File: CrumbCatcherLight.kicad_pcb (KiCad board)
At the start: 2 copper layers, 60.1 x 69.1 mm, 72 parts, among them J1 USB_C_Receptacle, J2 Conn_ARM_SWD_TagConnect_TC203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, Q1 2N7002VC-7, SW1 TL3780AF240QG, SW10 SW_SPST, SW11 PEC11R, SW2 PEC11R, SW3 SW_SPST, SW4 SW_SPST, SW5 PEC11R, SW6 SW_SPST, SW7 SW_SPST, SW9 SW_SPST, U1 ECMF02-2AMX6, U2 PCB, U3 XC6210B332MR, U4 GD25Q127CWIGR, U5 RP2040, Y1 12MHz

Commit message: Update BOM,
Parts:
- removed C14: 22pF, Capacitor_SMD:C_0402_1005Metric
- removed C28, C29: 100nF, Capacitor_SMD:C_0402_1005Metric
- removed the SW1 at (47.6, 36.1)
- removed TP1: Reset, TestPoint:TestPoint_Pad_D1.0mm
- removed TP2: Delay, TestPoint:TestPoint_Pad_D1.0mm
- removed TP3: Boot, TestPoint:TestPoint_Pad_D1.0mm
- removed U2: PCB, Mad_Footprints:BOM
- removed Y1: 12MHz, Crystal:Crystal_SMD_Abracon_ABM8G-4Pin_3.2x2.5mm
- added C22: 1uF, Capacitor_SMD:C_0603_1608Metric, B.Cu at (140.4, 83.0)
- added C23: 100nF, Capacitor_SMD:C_0402_1005Metric, B.Cu at (145.2, 74.1)
- added C24: 100nF, Capacitor_SMD:C_0402_1005Metric, B.Cu at (147.2, 74.1)
- added C25: 100nF, Capacitor_SMD:C_0402_1005Metric, B.Cu at (149.2, 74.1)
- added D11: SK6812_MINI_E, Mad_Footprints:SK6812_MINI_E, F.Cu at (139.5, 25.2)
- added D12: LL4148, Diode_SMD:D_MiniMELF, F.Cu at (146.8, 24.0)
- added D13: LL4148, Diode_SMD:D_MiniMELF, F.Cu at (146.8, 27.3)
- added D14: LL4148, Diode_SMD:D_MiniMELF, F.Cu at (146.8, 30.7)
- added D15: SK6812_MINI_E, Mad_Footprints:SK6812_MINI_E, F.Cu at (139.5, 31.0)
- added D16: SK6812_MINI_E, Mad_Footprints:SK6812_MINI_E, F.Cu at (139.5, 36.8)
- added D17: LL4148, Diode_SMD:D_MiniMELF, F.Cu at (146.8, 34.0)
- added D18: RB520S30, Diode_SMD:D_SOD-523, B.Cu at (105.6, 28.8)
- added R14: 27R, Resistor_SMD:R_0402_1005Metric, B.Cu at (120.1, 83.7)
- added SW10: TL3780AF240QG, Mad_Footprints:SW_TL3780AF240QG, B.Cu at (102.3, 31.3)
- added U0: PCB, Mad_Footprints:BOM, F.Cu at (154.0, 35.5)
- added X1: ECS-2520MVLC-120-CN, Mad_Footprints:Crystal_SMD_ECX-32-4Pin_3.2x2.5mm, B.Cu at (155.4, 78.2)
- C15: value 22pF -> 10uF; footprint Capacitor_SMD:C_0402_1005Metric -> Capacitor_SMD:C_0805_2012Metric
- C16: value 100nF -> 10uF; footprint Capacitor_SMD:C_0402_1005Metric -> Capacitor_SMD:C_0805_2012Metric
- C20: value 100nF -> 1uF; footprint Capacitor_SMD:C_0402_1005Metric -> Capacitor_SMD:C_0603_1608Metric
- C3, C4: footprint Capacitor_SMD:C_0402_1005Metric -> Capacitor_SMD:C_0805_2012Metric
- C5: value 4.7uF -> 10uF
- C6: value 10uF -> 100nF
- C7: value 10uF -> 100nF; footprint Capacitor_SMD:C_0805_2012Metric -> Capacitor_SMD:C_0402_1005Metric
- D1: value RB520S30 -> SK6812_MINI_E; footprint Diode_SMD:D_SOD-523 -> Mad_Footprints:WS2812C-2020
- D10, D5, D6: value LL4148 -> SK6812_MINI_E; footprint Diode_SMD:D_MiniMELF -> Mad_Footprints:SK6812_MINI_E
- D2: value LL4148 -> LED; footprint Diode_SMD:D_MiniMELF -> LED_SMD:LED_0603_1608Metric; moved to B.Cu
- R10: value 27R -> 1K
- R11: value 1K -> 10K
- R12: value 2K2 -> 1K
- R13: value 5K1 -> 27R
- R3: value 10K -> 2K2
- R4: value 10K -> 5K1
- R5: value 51K -> 2K2
- R6: value 100K -> 10K
- R8: value 1K -> 51K
- R9: value 27R -> 100K
- U3: value XC6210B332MR -> NCP1117-3.3_SOT223; footprint Package_TO_SOT_SMD:SOT-23-5 -> Package_TO_SOT_SMD:SOT-223-3_TabPin2
- moved D1 112.7 mm to (156.8, 74.2)
- moved C17 80.3 mm to (152.7, 74.3)
- moved C18 78.7 mm to (152.9, 73.2)
- moved C19 78.7 mm to (152.9, 75.2)
- moved C13 78.0 mm to (153.2, 77.9), turned to -90 degrees
- moved C5 76.4 mm to (124.4, 74.8), turned to 90 degrees
- moved C4 66.2 mm to (122.6, 81.4), turned to -90 degrees
- moved R5 65.4 mm to (111.5, 62.2), turned to -90 degrees
- moved R11 64.8 mm to (108.2, 27.4)
- moved C15 64.8 mm to (109.7, 27.9)
- moved U3 64.5 mm to (119.0, 76.0)
- moved R3 64.0 mm to (86.6, 92.5)
- moved C6 62.0 mm to (82.4, 45.0)
- moved R4 56.8 mm to (88.5, 92.5)
- moved R9 55.9 mm to (113.1, 29.6)
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- renumbered SW2 to SW1, SW3 to SW2, SW4 to SW3, SW5 to SW4, SW6 to SW5, SW7 to SW6, SW11 to SW7, SW9 to SW8, SW10 to SW9
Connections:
- net /2_SDA1 renamed /RP2040a/SDA1
- net /3_SCL1 renamed /RP2040a/SCL1
- net /DATA_RX0 renamed /RP2040a/RX0
- net /RP2040/GPIO10 renamed /RP2040a/IO_10
- net /RP2040/GPIO17 renamed /RP2040a/RP2040/GPIO17
- net /RP2040/GPIO18 renamed /RP2040a/RP2040/GPIO18
- net /RP2040/GPIO20 renamed /RP2040a/MISO
- net /RP2040/GPIO21 renamed /RP2040a/~{CS}
- net /RP2040/GPIO22 renamed /RP2040a/SCK
- net /RP2040/GPIO23 renamed /RP2040a/MOSI
- net /RP2040/GPIO24 renamed /RP2040a/RP2040/GPIO24
- net /RP2040/GPIO26 renamed /RP2040a/A0
- net /RP2040/GPIO27 renamed /RP2040a/A1
- net /RP2040/GPIO28 renamed /RP2040a/A2
- net /RP2040/GPIO29 renamed /RP2040a/A3
- net /RP2040/GPIO7 renamed /RP2040a/IO_7
- net /RP2040/GPIO8 renamed /RP2040a/IO_8
- net /RP2040/GPIO9 renamed /RP2040a/IO_9
- net /RP2040/QSPI_SCLK renamed /RP2040a/RP2040/QSPI_SCLK
- net /RP2040/QSPI_SD0 renamed /RP2040a/RP2040/QSPI_SD0
- net /RP2040/QSPI_SD1 renamed /RP2040a/RP2040/QSPI_SD1
- net /RP2040/QSPI_SD2 renamed /RP2040a/RP2040/QSPI_SD2
- net /RP2040/QSPI_SD3 renamed /RP2040a/RP2040/QSPI_SD3
- net /RP2040/SWCLK renamed /RP2040a/SWCLK
- net /RP2040/SWDIO renamed /RP2040a/SWDIO
- C10 pad 1: /RP2040/3V3 -> /RP2040a/ENC3A
- C11 pad 1: /RP2040/3V3 -> GND
- C11 pad 2: GND -> /RP2040a/ENC3B
- C12 pad 1: /RP2040/3V3 -> /RP2040a/3V3
- C13 pad 1: /RP2040/3V3 -> /RP2040a/3V3
- C15 pad 1: GND -> Net-(Q1B-G)
- C15 pad 2: Net-(C15-Pad2) -> GND
- C16 pad 1: /RP2040/3V3 -> Net-(Q1B-G)
- C17 pad 1: /RP2040/3V3 -> /RP2040a/3V3
- C18 pad 1: /RP2040/1V1 -> /RP2040a/3V3
- C19 pad 1: /RP2040/1V1 -> /RP2040a/3V3
- C20 pad 1: /RP2040/GPIO15 -> GND
- C20 pad 2: GND -> /RP2040a/RP2040/1V1
- C21 pad 1: GND -> /RP2040a/3V3
- C21 pad 2: /RP2040/GPIO16 -> GND
- C26 pad 1: /RP2040/GPIO13 -> /RP2040a/RP2040/1V1
- C27 pad 1: GND -> /RP2040a/RP2040/1V1
- C27 pad 2: /RP2040/GPIO14 -> GND
- C5 pad 1: Net-(Q1B-G) -> /RP2040a/3V3
- C6 pad 1: /RP2040/3V3 -> /RP2040a/ENC1A
- C7 pad 1: Net-(Q1B-G) -> GND
- C7 pad 2: GND -> /RP2040a/ENC1B
- C8 pad 1: /RP2040/3V3 -> /RP2040a/ENC2A
- C9 pad 1: /RP2040/3V3 -> GND
- C9 pad 2: GND -> /RP2040a/ENC2B
- D1 pad 1: Net-(D1-K) -> unconnected-(D1-DOUT-Pad1)
- D1 pad 2: Net-(D1-A) -> GND
- D10 pad 1: /RP2040/GPIO6 -> +5V
- D10 pad 2: Net-(D10-A) -> Net-(D10-DOUT)
- D2 pad 1: /RP2040/GPIO4 -> GND
- D3 pad 1: /RP2040/GPIO5 -> /RP2040a/IO_5
- D4 pad 1: /RP2040/GPIO6 -> /RP2040a/IO_6
- D5 pad 1: /RP2040/GPIO4 -> +5V
- D5 pad 2: Net-(D5-A) -> Net-(D10-DIN)
- D6 pad 1: /RP2040/GPIO5 -> +5V
- D6 pad 2: Net-(D6-A) -> Net-(D11-DIN)
- D7 pad 1: /RP2040/GPIO6 -> /RP2040a/IO_4
- D8 pad 1: /RP2040/GPIO4 -> /RP2040a/IO_5
- D9 pad 1: /RP2040/GPIO5 -> /RP2040a/IO_6
- J2 pad 1: /RP2040/3V3 -> /RP2040a/3V3
- J2 pad 3: /RP2040/~{RST} -> /RP2040a/~{RST}
- Q1 pad 2: Net-(D1-A) -> Net-(D18-A)
- Q1 pad 6: /RP2040/~{RST} -> /RP2040a/~{RST}
- R10 pad 1: /RP2040/USB_D- -> /RP2040a/RP2040/XTAL_IN
- R10 pad 2: Net-(U5-D-) -> Net-(X1-OUT)
- R11 pad 1: Net-(C15-Pad2) -> /RP2040a/RP2040/QSPI_~{CS}
- R11 pad 2: Net-(U5-XTAL_OUT) -> /RP2040a/3V3
- R12 pad 1: VBUS -> Net-(Q1B-S)
- R12 pad 2: /RP2040/VBUS_DETECT -> /RP2040a/RP2040/QSPI_~{CS}
- R13 pad 1: /RP2040/VBUS_DETECT -> /RP2040a/USB_D+
- R13 pad 2: GND -> Net-(U5-D+)
- R3 pad 1: GND -> VBUS
- R3 pad 2: Net-(D1-A) -> /RP2040a/VBUS_DETECT
- R4 pad 1: /RP2040/~{RST} -> /RP2040a/VBUS_DETECT
- R4 pad 2: /RP2040/3V3 -> GND
- R5 pad 1: Net-(Q1B-G) -> /RP2040a/3V3
- R5 pad 2: Net-(D1-K) -> Net-(D2-A)
- R6 pad 2: Net-(Q1B-G) -> Net-(D18-A)
- R7 pad 1: /RP2040/QSPI_nCS -> /RP2040a/~{RST}
- R7 pad 2: /RP2040/3V3 -> /RP2040a/3V3
- R8 pad 1: Net-(Q1B-S) -> Net-(Q1B-G)
- R8 pad 2: /RP2040/QSPI_nCS -> Net-(D18-K)
- R9 pad 1: /RP2040/USB_D+ -> GND
- R9 pad 2: Net-(U5-D+) -> Net-(Q1B-G)
- SW1 pad A: /RP2040/GPIO11 -> /RP2040a/ENC1A
- SW1 pad B: /RP2040/GPIO12 -> /RP2040a/ENC1B
- SW1 pad S2: Net-(D2-A) -> Net-(D7-A)
- SW4 pad A: /RP2040/GPIO13 -> /RP2040a/ENC2A
- SW4 pad B: /RP2040/GPIO14 -> /RP2040a/ENC2B
- SW4 pad S2: Net-(D5-A) -> Net-(D12-A)
- SW5 pad 1: Net-(D7-A) -> Net-(D9-A)
- SW6 pad 1: Net-(D6-A) -> Net-(D8-A)
- SW7 pad A: /RP2040/GPIO15 -> /RP2040a/ENC3A
- SW7 pad B: /RP2040/GPIO16 -> /RP2040a/ENC3B
- SW7 pad S2: Net-(D8-A) -> Net-(D17-A)
- SW8 pad 1: Net-(D9-A) -> Net-(D13-A)
- SW9 pad 1: Net-(D10-A) -> Net-(D14-A)
- U1 pad 5: /RP2040/USB_D+ -> /RP2040a/USB_D-
- U1 pad 6: /RP2040/USB_D- -> /RP2040a/USB_D+
- U3 pad 1: +5V -> GND
- U3 pad 2: GND -> /RP2040a/3V3
- U4 pad 1: /RP2040/QSPI_nCS -> /RP2040a/RP2040/QSPI_~{CS}
- U4 pad 8: /RP2040/3V3 -> /RP2040a/3V3
- U5 pad 1: /RP2040/3V3 -> /RP2040a/3V3
- U5 pad 10: /RP2040/3V3 -> /RP2040a/3V3
- U5 pad 14: /RP2040/GPIO11 -> /RP2040a/ENC1A
- U5 pad 15: /RP2040/GPIO12 -> /RP2040a/ENC1B
- U5 pad 16: /RP2040/GPIO13 -> /RP2040a/ENC2A
- U5 pad 17: /RP2040/GPIO14 -> /RP2040a/ENC2B
- U5 pad 18: /RP2040/GPIO15 -> /RP2040a/ENC3A
- U5 pad 2: /LED_TX0 -> /RP2040a/TX0
- U5 pad 20: Net-(U5-XTAL_IN) -> /RP2040a/RP2040/XTAL_IN
- U5 pad 21: Net-(U5-XTAL_OUT) -> unconnected-(U5-XTAL_OUT-Pad21)
- U5 pad 22: /RP2040/3V3 -> /RP2040a/3V3
- U5 pad 23: /RP2040/1V1 -> /RP2040a/RP2040/1V1
- U5 pad 26: /RP2040/~{RST} -> /RP2040a/~{RST}
- U5 pad 27: /RP2040/GPIO16 -> /RP2040a/ENC3B
- U5 pad 30: /RP2040/VBUS_DETECT -> /RP2040a/VBUS_DETECT
- U5 pad 33: /RP2040/3V3 -> /RP2040a/3V3
- U5 pad 37: /RP2040/GPIO25 -> /RP2040a/STATUS_LED_DO
- U5 pad 42: /RP2040/3V3 -> /RP2040a/3V3
- U5 pad 43: /RP2040/3V3 -> /RP2040a/3V3
- U5 pad 44: /RP2040/3V3 -> /RP2040a/3V3
- U5 pad 45: /RP2040/1V1 -> /RP2040a/RP2040/1V1
- U5 pad 48: /RP2040/3V3 -> /RP2040a/3V3
- U5 pad 49: /RP2040/3V3 -> /RP2040a/3V3
- U5 pad 50: /RP2040/1V1 -> /RP2040a/RP2040/1V1
- U5 pad 56: /RP2040/QSPI_nCS -> /RP2040a/RP2040/QSPI_~{CS}
- U5 pad 6: /RP2040/GPIO4 -> /RP2040a/IO_4
- U5 pad 7: /RP2040/GPIO5 -> /RP2040a/IO_5
- U5 pad 8: /RP2040/GPIO6 -> /RP2040a/IO_6
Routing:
- net Net-(U5-XTAL_IN): track 8.23 -> 0.00 mm
- net /RP2040a/3V3: track 0.00 -> 3.18 mm
- net Net-(C15-Pad2): track 2.89 -> 0.00 mm
- net GND: track 6.16 -> 3.47 mm
- net Net-(U5-XTAL_OUT): track 1.93 -> 0.00 mm
- net /RP2040a/RP2040/XTAL_IN: track 0.00 -> 1.55 mm
- net Net-(X1-OUT): track 0.00 -> 1.27 mm

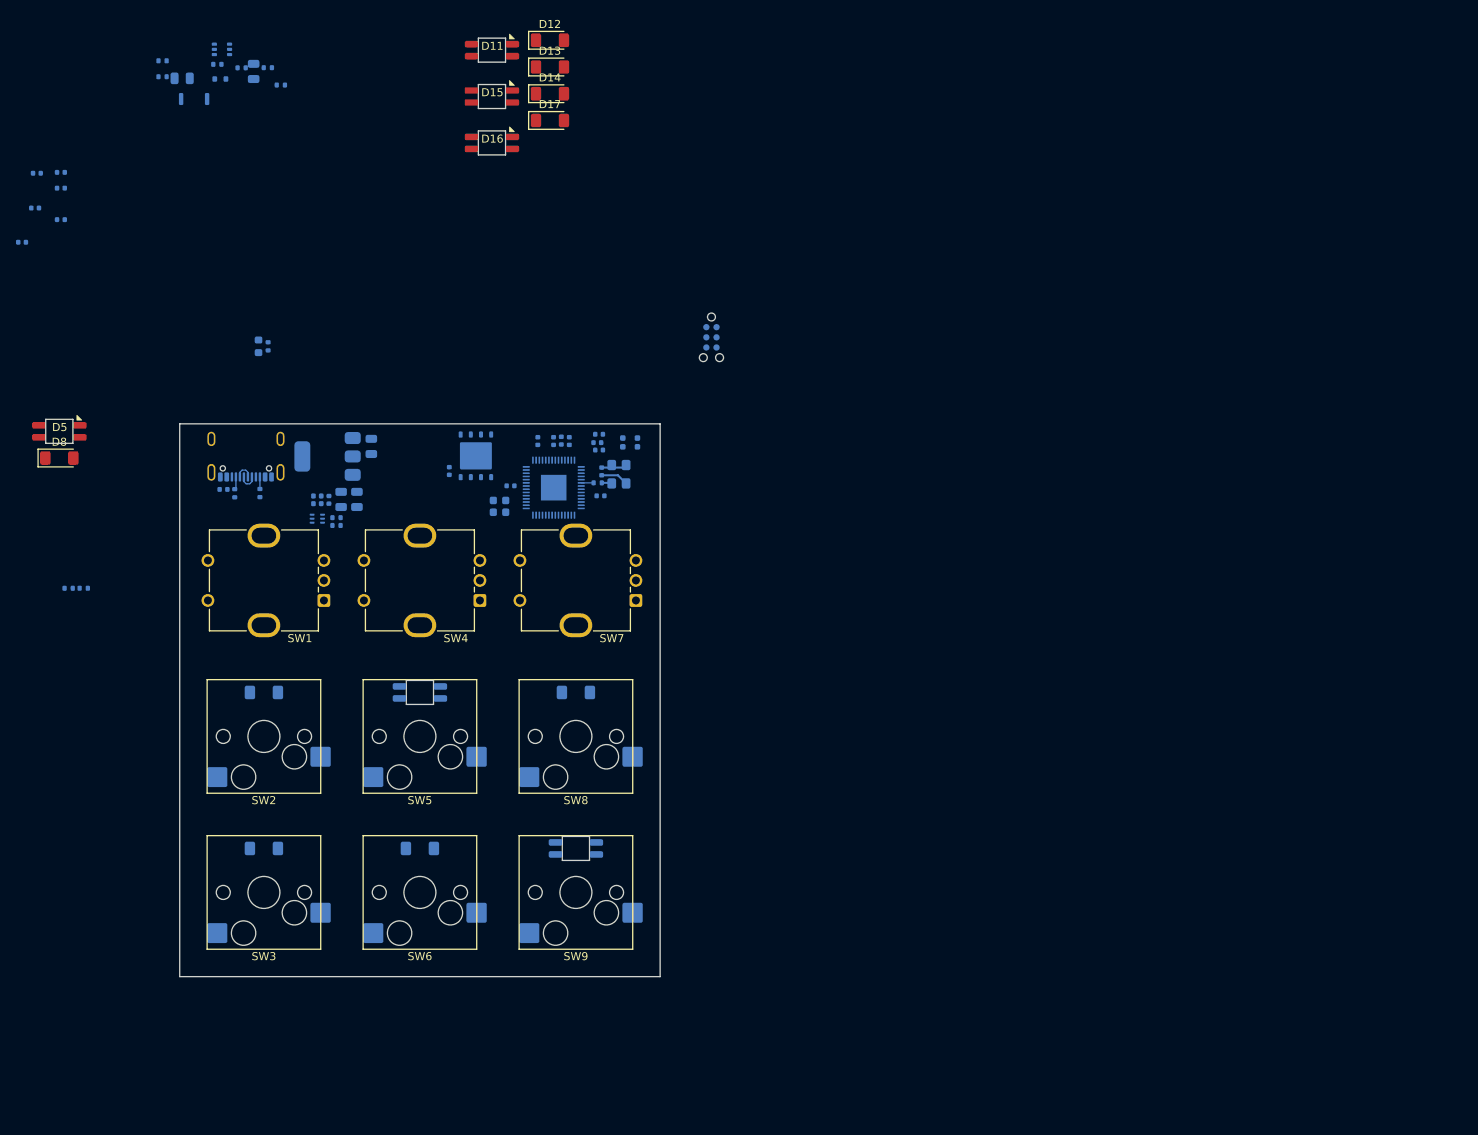
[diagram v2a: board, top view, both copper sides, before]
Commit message: Update to nRF52840 module, add BQ for battery charging
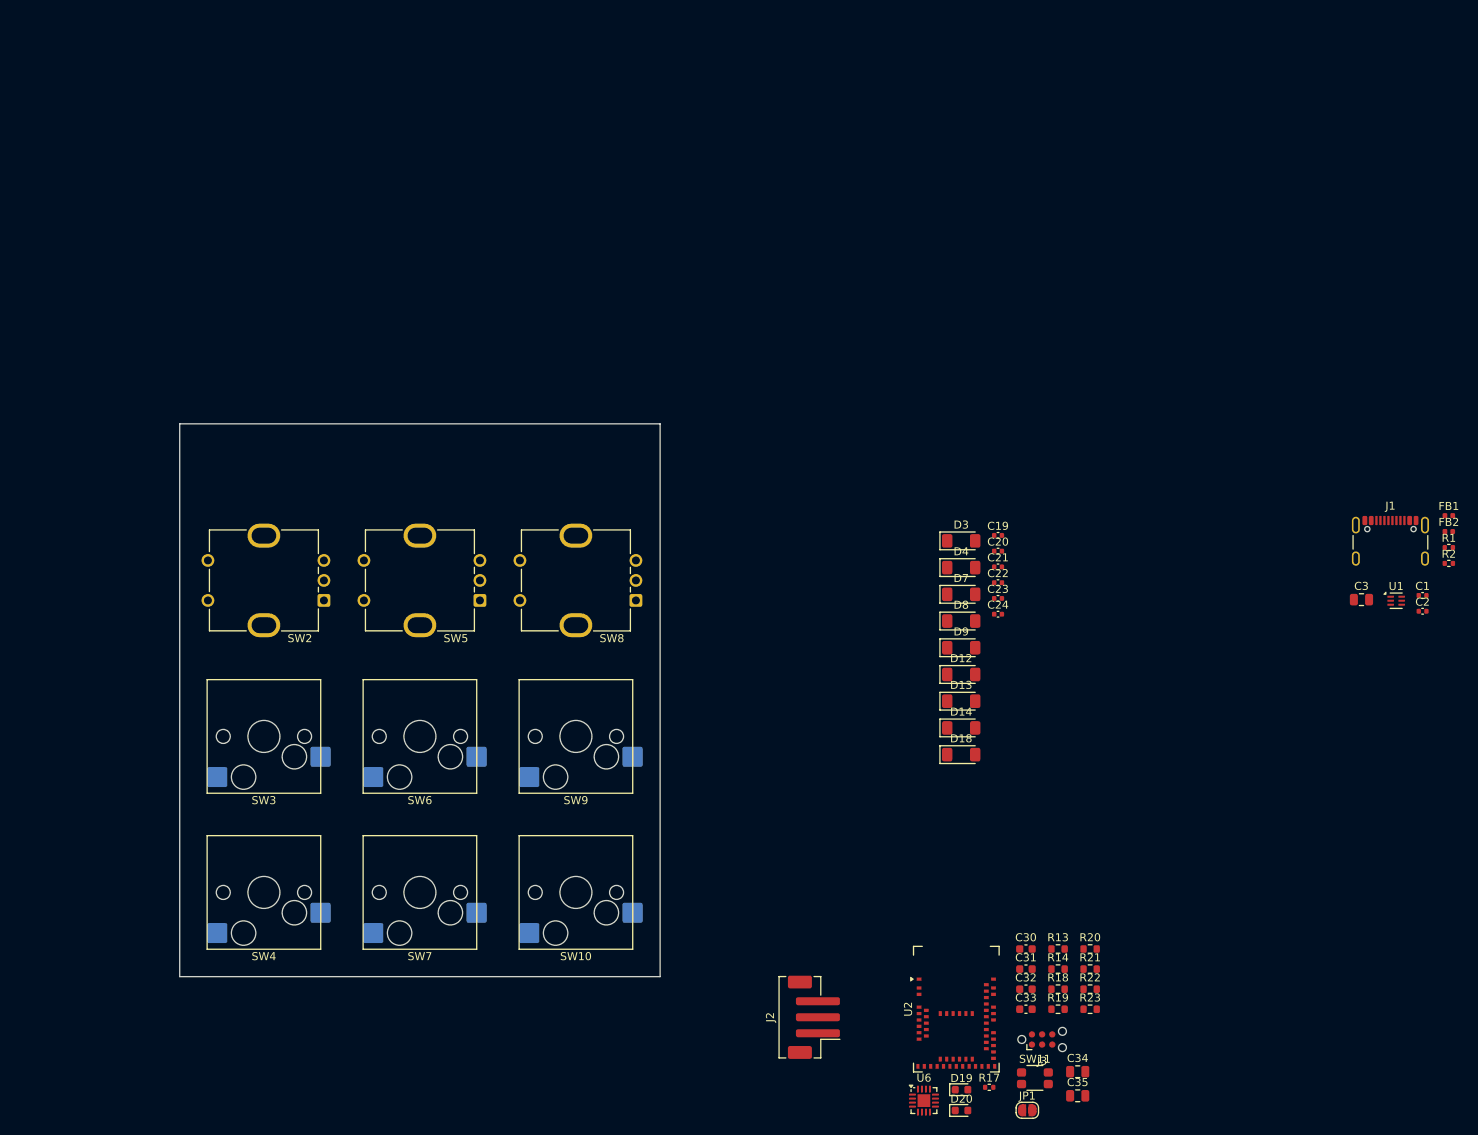
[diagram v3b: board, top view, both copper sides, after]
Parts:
- removed C10, C11, C12, C13, C17, C18, C25, C26, C27, C6, C7, C8, C9: 100nF, Capacitor_SMD:C_0402_1005Metric
- removed C15, C16, C4, C5: 10uF, Capacitor_SMD:C_0805_2012Metric
- removed D1: SK6812_MINI_E, Mad_Footprints:WS2812C-2020
- removed D10, D11, D15, D16, D5, D6: SK6812_MINI_E, Mad_Footprints:SK6812_MINI_E
- removed D17: LL4148, Diode_SMD:D_MiniMELF
- removed D2: LED, LED_SMD:LED_0603_1608Metric
- removed Q1: 2N7002VC-7, Package_TO_SOT_SMD:SOT-363_SC-70-6
- removed R10, R12: 1K, Resistor_SMD:R_0402_1005Metric
- removed R11, R6, R7: 10K, Resistor_SMD:R_0402_1005Metric
- removed R3, R5: 2K2, Resistor_SMD:R_0402_1005Metric
- removed R4: 5K1, Resistor_SMD:R_0402_1005Metric
- removed R8: 51K, Resistor_SMD:R_0402_1005Metric
- removed R9: 100K, Resistor_SMD:R_0402_1005Metric
- removed the SW10 at (102.3, 31.3)
- removed U3: NCP1117-3.3_SOT223, Package_TO_SOT_SMD:SOT-223-3_TabPin2
- removed U4: GD25Q127CWIGR, Mad_Footprints:GD25LQ128DYIGR
- removed U5: RP2040, Package_DFN_QFN:QFN-56-1EP_7x7mm_P0.4mm_EP3.2x3.2mm
- removed X1: ECS-2520MVLC-120-CN, Mad_Footprints:Crystal_SMD_ECX-32-4Pin_3.2x2.5mm
- added C30: 8pF, Capacitor_SMD:C_0603_1608Metric, F.Cu at (206.3, 137.6)
- added C31: 8pF, Capacitor_SMD:C_0603_1608Metric, F.Cu at (206.3, 140.1)
- added C32: 1uF, Capacitor_SMD:C_0603_1608Metric, F.Cu at (206.3, 142.6)
- added C33: 100nF, Capacitor_SMD:C_0603_1608Metric, F.Cu at (206.3, 145.1)
- added C34: 4.7uF, Capacitor_SMD:C_0805_2012Metric, F.Cu at (212.7, 152.9)
- added C35: 4.7uF, Capacitor_SMD:C_0805_2012Metric, F.Cu at (212.7, 155.9)
- added D19: Yellow, LED_SMD:LED_0603_1608Metric, F.Cu at (198.2, 155.2)
- added D20: GREEN, LED_SMD:LED_0603_1608Metric, F.Cu at (198.2, 157.8)
- added J3: Conn_ARM_SWD_TagConnect_TC2030-NL, Connector:Tag-Connect_TC2030-IDC-NL_2x03_P1.27mm_Vertical, F.Cu at (208.3, 148.9)
- added JP1: Charge Boost, Jumper:SolderJumper-2_P1.3mm_Open_RoundedPad1.0x1.5mm, F.Cu at (206.4, 157.7)
- added R17: 1K, Resistor_SMD:R_0402_1005Metric, F.Cu at (201.7, 154.9)
- added R18: 1K, Resistor_SMD:R_0603_1608Metric, F.Cu at (210.3, 142.6)
- added R19: 1K, Resistor_SMD:R_0603_1608Metric, F.Cu at (210.3, 145.1)
- added R20: 10K, Resistor_SMD:R_0603_1608Metric, F.Cu at (214.3, 137.6)
- added R21: 10K, Resistor_SMD:R_0603_1608Metric, F.Cu at (214.3, 140.1)
- added R22: 10K, Resistor_SMD:R_0603_1608Metric, F.Cu at (214.3, 142.6)
- added R23: 1K, Resistor_SMD:R_0603_1608Metric, F.Cu at (214.3, 145.1)
- added SW11: EVPAA202K, Mad_Footprints:EVP-AA202K, F.Cu at (207.4, 153.7)
- added U2: MDBT50Q-U1MV2, Mad_Footprints:Raytac_MDBT50Q, F.Cu at (197.6, 145.1)
- added U6: BQ24075RGT, Package_DFN_QFN:VQFN-16-1EP_3x3mm_P0.5mm_EP1.6x1.6mm, F.Cu at (193.5, 156.5)
- C1, C19, C2, C21, C23, C24, C3, D3, D4, D7, D9, FB1, FB2, J1, R1, R2, U1: moved to F.Cu
- C20, C22: value 1uF -> 100nF; footprint Capacitor_SMD:C_0603_1608Metric -> Capacitor_SMD:C_0402_1005Metric; moved to F.Cu
- D18: value RB520S30 -> LL4148; footprint Diode_SMD:D_SOD-523 -> Diode_SMD:D_MiniMELF; moved to F.Cu
- J2: value Conn_ARM_SWD_TagConnect_TC2030-NL -> Conn_01x03; footprint Connector:Tag-Connect_TC2030-IDC-NL_2x03_P1.27mm_Vertical -> Connector_JST:JST_PH_B3B-PH-SM4-TB_1x03-1MP_P2.00mm_Vertical; moved to F.Cu
- R13: value 27R -> 2M; footprint Resistor_SMD:R_0402_1005Metric -> Resistor_SMD:R_0603_1608Metric; moved to F.Cu
- R14: value 27R -> 806k; footprint Resistor_SMD:R_0402_1005Metric -> Resistor_SMD:R_0603_1608Metric; moved to F.Cu
- moved R1 151.9 mm to (259.1, 87.4), turned to 0 degrees
- moved C1 150.5 mm to (255.8, 93.4), turned to 0 degrees
- moved R2 148.9 mm to (259.1, 89.4), turned to 0 degrees
- moved J1 143.6 mm to (251.8, 87.7)
- moved FB2 141.5 mm to (259.1, 85.4)
- moved FB1 141.5 mm to (259.1, 83.4)
- moved C2 137.4 mm to (255.8, 95.3), turned to 0 degrees
- moved U1 135.2 mm to (252.5, 94.0)
- moved C3 128.2 mm to (248.2, 93.9), turned to 0 degrees
- moved D18 125.3 mm to (198.2, 113.3), turned to 0 degrees
- moved U0 120.3 mm to (236.7, 123.0)
- moved D8 114.6 mm to (198.2, 96.6)
- moved R14 106.4 mm to (210.3, 140.1)
- moved R13 104.6 mm to (210.3, 137.6)
- moved D12 94.5 mm to (198.2, 103.3)
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- renumbered SW9 to SW10, SW1 to SW2, SW2 to SW3, SW3 to SW4, SW4 to SW5, SW5 to SW6, SW6 to SW7, SW7 to SW8, SW8 to SW9
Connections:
- net /RP2040a/IO_5 renamed /Switches/Row1
- net /RP2040a/IO_6 renamed /Switches/Row2
- net /RP2040a/IO_7 renamed /Switches/Col0
- net /RP2040a/IO_8 renamed /Switches/Col1
- net /RP2040a/IO_9 renamed /Switches/Col2
- C19 pad 1: /RP2040a/3V3 -> /Switches/ENC1A
- C20 pad 2: /RP2040a/RP2040/1V1 -> /Switches/ENC1B
- C21 pad 1: /RP2040a/3V3 -> /Switches/ENC2A
- C22 pad 2: /RP2040a/3V3 -> /Switches/ENC2B
- C23 pad 1: /RP2040a/3V3 -> /Switches/ENC3A
- C24 pad 1: /RP2040a/3V3 -> GND
- C24 pad 2: GND -> /Switches/ENC3B
- D12 pad 1: /RP2040a/IO_4 -> /Switches/Row0
- D18 pad 1: Net-(D18-K) -> /Switches/Row0
- D7 pad 1: /RP2040a/IO_4 -> /Switches/Row0
- J2 pad 1: /RP2040a/3V3 -> GND
- J2 pad 2: /RP2040a/SWDIO -> /nRF52840/VBAT
- J2 pad 3: /RP2040a/~{RST} -> GND
- R13 pad 1: /RP2040a/USB_D+ -> GND
- R13 pad 2: Net-(U5-D+) -> /nRF52840/BVOLT
- R14 pad 1: /RP2040a/USB_D- -> /nRF52840/BVOLT
- R14 pad 2: Net-(U5-D-) -> /nRF52840/VBAT
- SW2 pad A: /RP2040a/ENC1A -> /Switches/ENC1A
- SW2 pad B: /RP2040a/ENC1B -> /Switches/ENC1B
- SW5 pad A: /RP2040a/ENC2A -> /Switches/ENC2A
- SW5 pad B: /RP2040a/ENC2B -> /Switches/ENC2B
- SW8 pad A: /RP2040a/ENC3A -> /Switches/ENC3A
- SW8 pad B: /RP2040a/ENC3B -> /Switches/ENC3B
- SW8 pad S2: Net-(D17-A) -> Net-(D18-A)
- U1 pad 5: /RP2040a/USB_D- -> /nRF52840/USB_D_P
- U1 pad 6: /RP2040a/USB_D+ -> /nRF52840/USB_D_N
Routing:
- net GND: track 3.47 -> 0.00 mm
- net /RP2040a/3V3: track 3.18 -> 0.00 mm
- net Net-(U1-D+_in): track 2.38 -> 0.00 mm
- net Net-(U1-D-_in): track 2.38 -> 0.00 mm
- net Net-(J1-CC1): track 1.59 -> 0.00 mm
- net /RP2040a/RP2040/XTAL_IN: track 1.55 -> 0.00 mm
- net Net-(J1-CC2): track 1.50 -> 0.00 mm
- net Net-(X1-OUT): track 1.27 -> 0.00 mm
